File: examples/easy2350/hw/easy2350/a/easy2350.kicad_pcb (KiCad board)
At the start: 4 copper layers, 21 x 51 mm, 58 parts, among them J1 USB-C, J2 GPIO left, J3 GPIO right, J4 SWD, SW1 BOOTSEL, SW2 RESET, U1 RP2350A, U2 USBLC6-2SC6, U3 AP7361C-33FGE, U4 SN74LV1T125DBVR, U5 W25Q128JVSIQ, Y1 12MHz

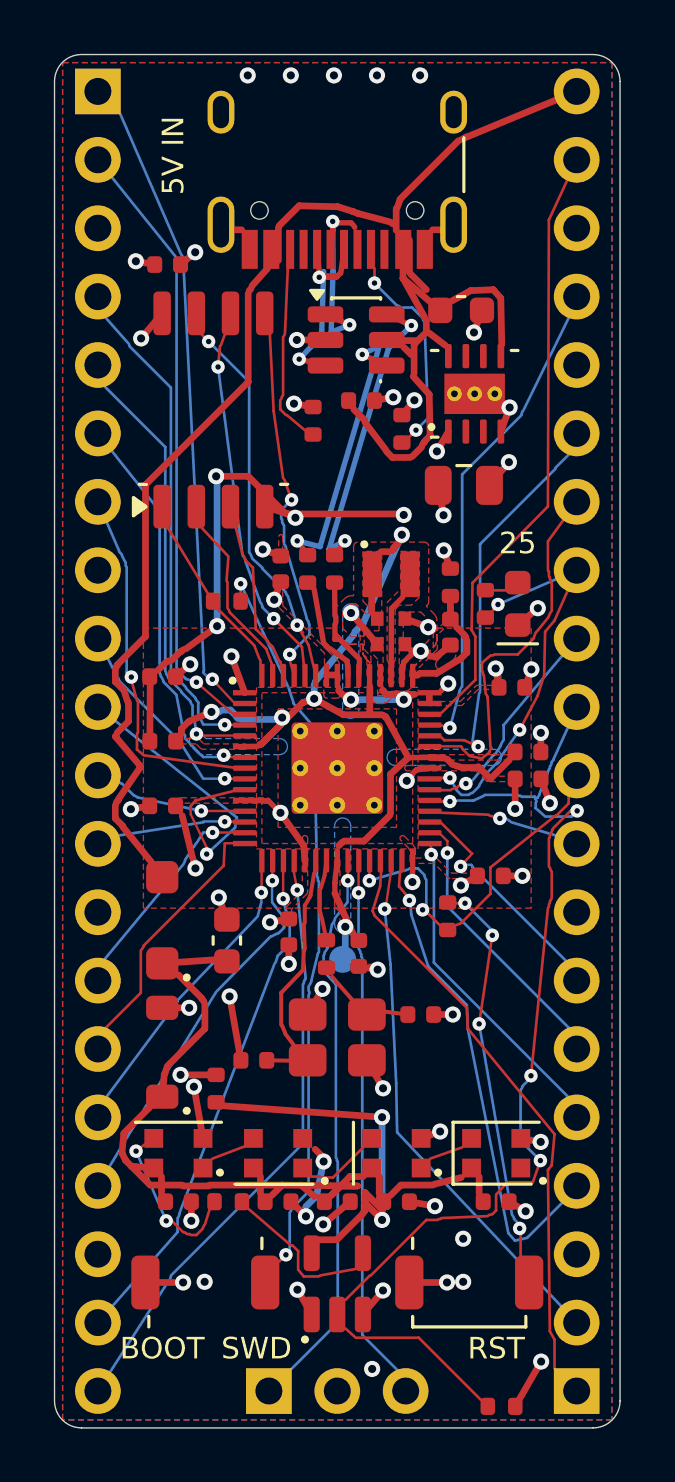
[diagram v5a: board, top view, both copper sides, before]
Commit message: easy2350: re-routed on ultraroute 5064384, every track ends inside its pad
pad_joints.py passes (205 SMD pads, no thin joints; J1.B7 and R6.1 failed
before). DRC 0 errors, 0 unconnected, parity 0. Still 7 isolated +1V1
reference-zone pieces, waiting on ultraroute joining zone islands with vias.

Co-Authored-By: Claude Opus 5.5 <noreply@anthropic.com>
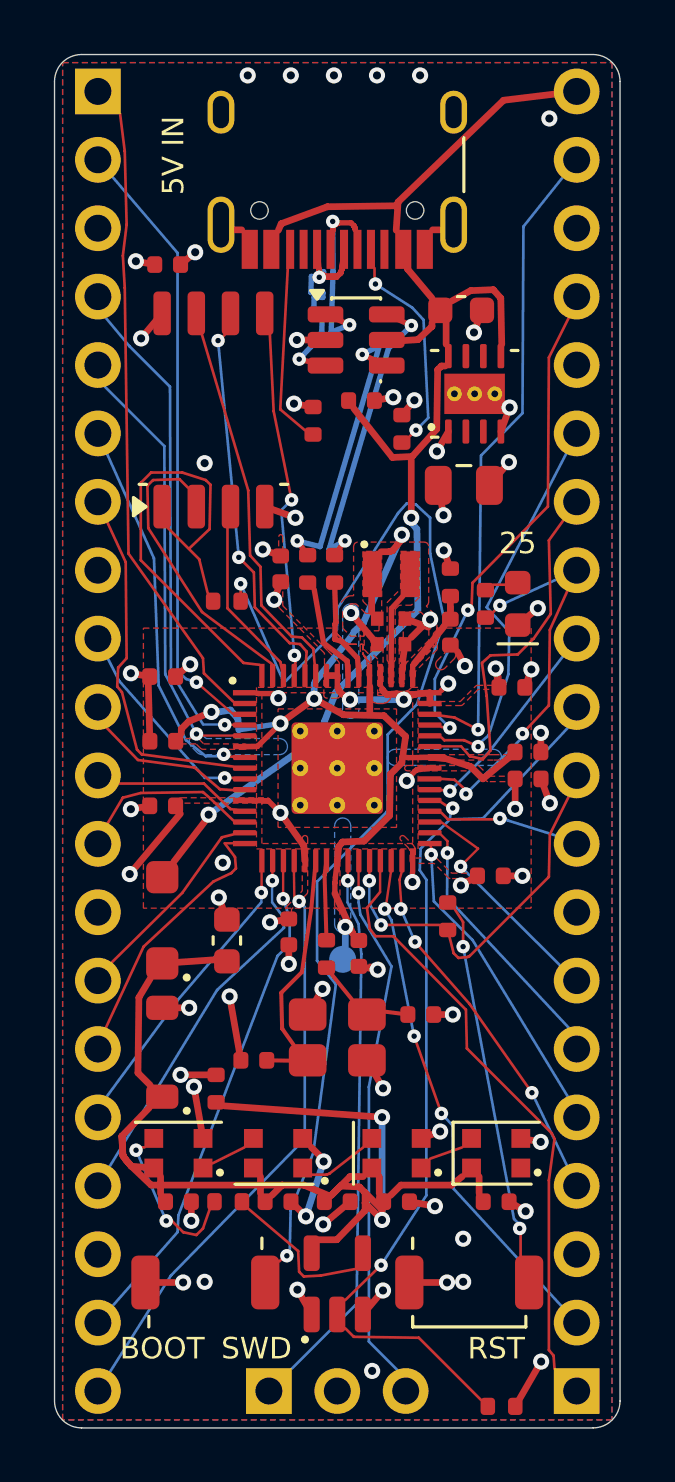
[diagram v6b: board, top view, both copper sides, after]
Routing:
- net Net-(R7-Pad2): track 26.2 -> 43.7 mm
- net GND: track 62.3 -> 48.7 mm
- net VBUS: track 59.7 -> 47.8 mm, vias 0 -> 2
- net /QSPI_SS: track 5.39 -> 17.3 mm
- net /GPIO7: track 12.2 -> 5.51 mm, vias 1 -> 0
- net /GPIO23: track 37.6 -> 32.3 mm, vias 4 -> 2
- net /QSPI_SD1: track 5.89 -> 10.2 mm
- net /GPIO18: track 17.0 -> 13.7 mm, vias 1 -> 3
- net /USB_DP_C: track 7.90 -> 10.8 mm
- net /GPIO9: track 4.29 -> 6.48 mm, vias 1 -> 0
- net /RUN: track 11.3 -> 13.1 mm
- net +3V3: track 23.9 -> 25.6 mm, vias 20 -> 21
- net +1V1: track 34.1 -> 35.8 mm
- net /GPIO29: track 22.5 -> 24.0 mm, vias 0 -> 1
- net /VREG_AVDD: track 3.92 -> 2.65 mm
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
